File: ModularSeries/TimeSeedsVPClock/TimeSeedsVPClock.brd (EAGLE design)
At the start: 92 x 47 mm, 75 parts, among them T1 2N3904

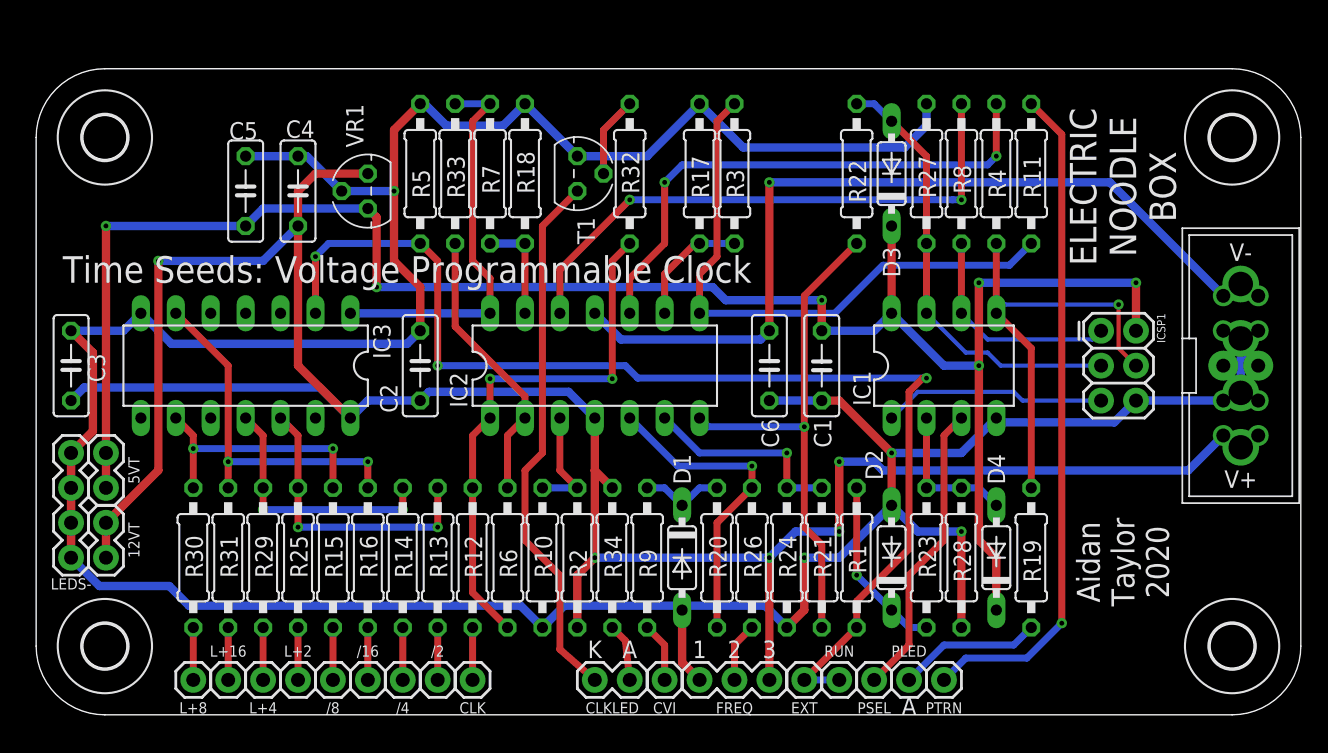
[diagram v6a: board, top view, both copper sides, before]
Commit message: BOM, panel wiring and documentation complete for TimeSeed
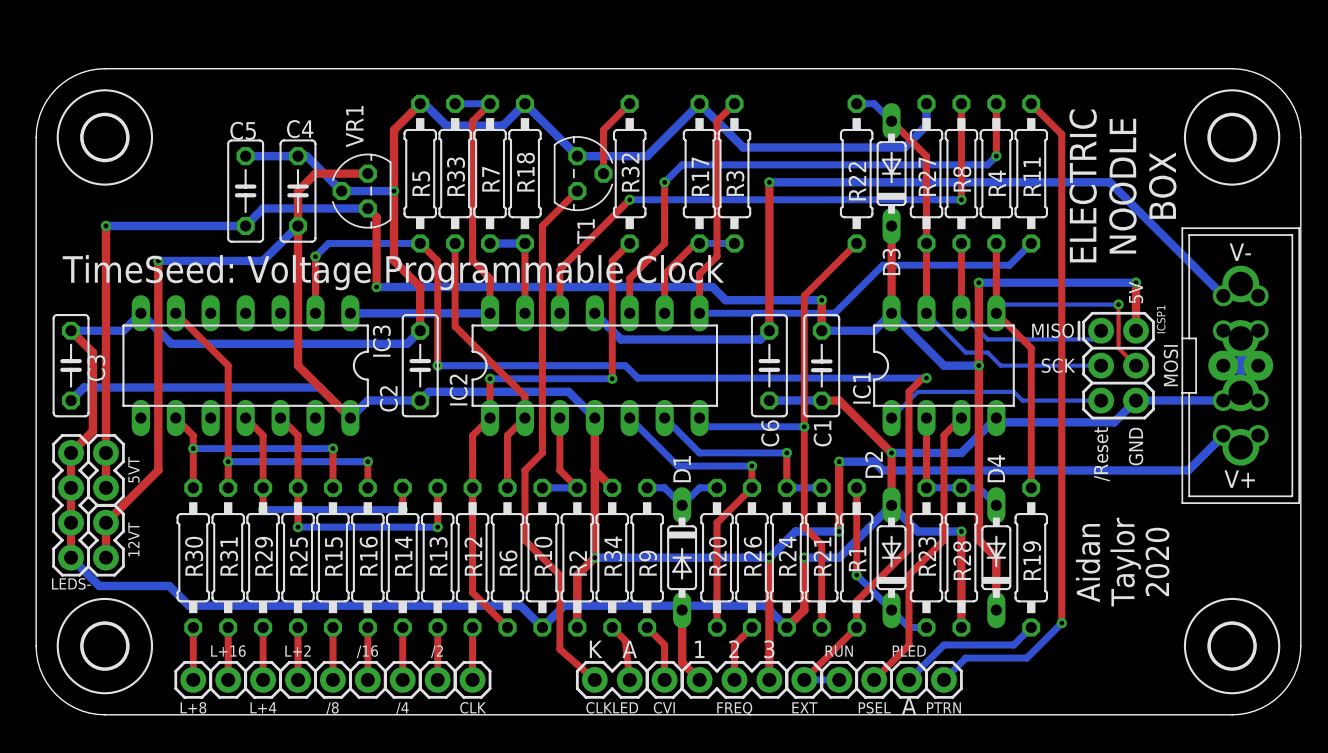
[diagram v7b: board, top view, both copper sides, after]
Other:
- board text added: "/Reset"
- board text added: "5V"
- board text added: "GND"
- board text added: "MISO"
- board text added: "MOSI"
- board text added: "SCK"
- board text added: "TimeSeed: Voltage Programmable Clock"
- board text removed: "Time Seeds: Voltage Programmable Clock"
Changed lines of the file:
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@@
 <wire x1="0" y1="5" x2="0" y2="42" width="0" layer="20"/>
 <wire x1="0" y1="42" x2="5" y2="47" width="0" layer="20" curve="-90"/>
-<text x="1.9375" y="31.4325" size="1.9304" layer="21" font="vector" ratio="16">Time Seeds: Voltage Programmable Clock</text>
+<text x="1.9375" y="31.4325" size="1.9304" layer="21" font="vector" ratio="16">TimeSeed: Voltage Programmable Clock</text>
 <text x="79.0575" y="38.4175" size="1.9304" layer="21" font="vector" ratio="16" rot="R90" align="center">ELECTRIC
 NOODLE
@@
 <dimension x1="5" y1="5" x2="5" y2="42" x3="-1" y3="23.5" textsize="1.778" layer="49"/>
 <dimension x1="0" y1="0" x2="0" y2="47" x3="-4" y3="23.5" textsize="1.778" layer="49"/>
+<text x="77.47" y="20.955" size="1.016" layer="21" font="vector" rot="R270" align="center-left">/Reset</text>
+<text x="80.01" y="20.955" size="1.016" layer="21" font="vector" rot="R270" align="center-left">GND</text>
+<text x="75.565" y="25.4" size="1.016" layer="21" font="vector" rot="R180" align="center-left">SCK</text>
+<text x="75.565" y="27.94" size="1.016" layer="21" font="vector" rot="R180" align="center-left">MISO</text>
+<text x="80.01" y="29.845" size="1.016" layer="21" font="vector" rot="R90" align="center-left">5V</text>
+<text x="82.55" y="25.4" size="1.016" layer="21" font="vector" rot="R90" align="center">MOSI</text>
 </plain>
 <attributes>
@@
 </element>
 <element name="ICSP1" library="ElectricNoodleBox" package="2X3" value="ICSP_2.54" x="77.47" y="27.94" smashed="yes" rot="R270">
-<attribute name="NAME" x="81.534" y="29.21" size="0.6096" layer="25" font="vector" ratio="20" rot="R270"/>
+<attribute name="NAME" x="81.534" y="29.845" size="0.6096" layer="25" font="vector" ratio="20" rot="R270"/>
 <attribute name="VALUE" x="75.057" y="29.21" size="0.6096" layer="27" font="vector" ratio="20" rot="R270"/>
 </element>

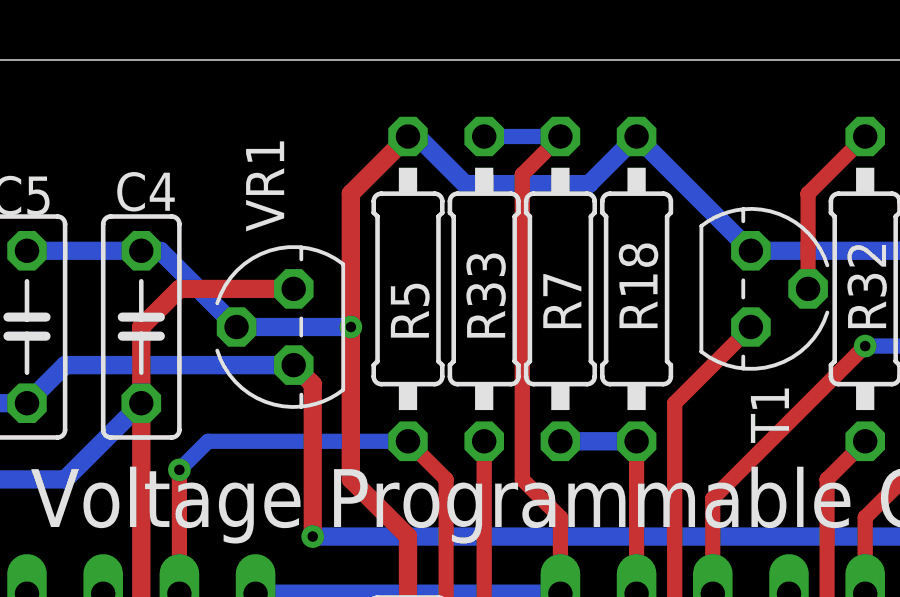
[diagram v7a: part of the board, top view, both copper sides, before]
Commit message: Pulse output fixed on Knives, schematics and layout updated. Panel added for Portals
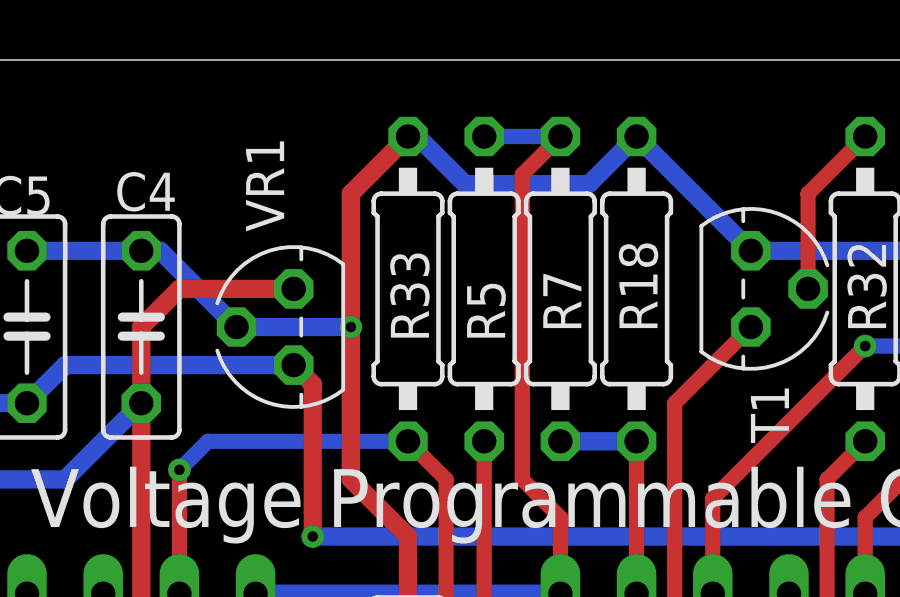
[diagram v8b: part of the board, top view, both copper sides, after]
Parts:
- R1: value 1K -> 470Ω
- R33: value 10K -> 100K
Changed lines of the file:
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@@
 <attribute name="VALUE" x="64.77" y="1.016" size="0.8128" layer="27" font="vector" ratio="20" align="top-left"/>
 </element>
-<element name="R1" library="rcl" library_urn="urn:adsk.eagle:library:334" package="0207/10" package3d_urn="urn:adsk.eagle:package:23491/2" value="1K" x="59.69" y="11.43" smashed="yes" rot="R270">
+<element name="R1" library="rcl" library_urn="urn:adsk.eagle:library:334" package="0207/10" package3d_urn="urn:adsk.eagle:package:23491/2" value="470Ω" x="59.69" y="11.43" smashed="yes" rot="R270">
 <attribute name="NAME" x="60.3885" y="10.287" size="1.27" layer="25" ratio="10" rot="R90"/>
 <attribute name="POPULARITY" value="81" x="30.48" y="-49.53" size="1.778" layer="27" rot="R270" display="off"/>
@@
 </element>
 <element name="R5" library="rcl" library_urn="urn:adsk.eagle:library:334" package="0207/10" package3d_urn="urn:adsk.eagle:package:23491/2" value="10K" x="30.48" y="39.37" smashed="yes" rot="R90">
-<attribute name="NAME" x="28.6385" y="37.592" size="1.27" layer="25" ratio="10" rot="R90"/>
+<attribute name="NAME" x="31.1785" y="37.592" size="1.27" layer="25" ratio="10" rot="R90"/>
 <attribute name="POPULARITY" value="81" x="67.31" y="83.82" size="1.778" layer="27" rot="R90" display="off"/>
 <attribute name="SPICEPREFIX" value="R" x="67.31" y="83.82" size="1.778" layer="27" rot="R90" display="off"/>
@@
 <attribute name="VALUE" x="25.4" y="41.275" size="1.27" layer="27" ratio="10" rot="R90"/>
 </element>
-<element name="R33" library="rcl" library_urn="urn:adsk.eagle:library:334" package="0207/10" package3d_urn="urn:adsk.eagle:package:23491/2" value="10K" x="27.94" y="39.37" smashed="yes" rot="R270">
-<attribute name="NAME" x="31.1785" y="37.592" size="1.27" layer="25" ratio="10" rot="R90"/>
+<element name="R33" library="rcl" library_urn="urn:adsk.eagle:library:334" package="0207/10" package3d_urn="urn:adsk.eagle:package:23491/2" value="100K" x="27.94" y="39.37" smashed="yes" rot="R270">
+<attribute name="NAME" x="28.6385" y="37.592" size="1.27" layer="25" ratio="10" rot="R90"/>
 <attribute name="POPULARITY" value="81" x="27.94" y="39.37" size="1.778" layer="27" rot="R270" display="off"/>
 <attribute name="SPICEPREFIX" value="R" x="27.94" y="39.37" size="1.778" layer="27" rot="R270" display="off"/>
